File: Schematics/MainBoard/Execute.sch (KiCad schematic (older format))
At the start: 7 parts, among them J23 Control Word LED Connector [1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, J24 Control Word LED Connector [8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, J25 Control Word LED Connector [0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, J5 C Register LED Connector, J6 Control Word LED Connector [2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, U48 74LS245

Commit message: The ALU Carry Input comes from a control signal instead of the C register.
So now:
  * C[0..3] --> S[0..3]
  * C4 --> M
  * ~CarryIn --> Cn
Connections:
- net ControlWord26 renamed ~CarryIn
- no-connect marks 5 -> 4
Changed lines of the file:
@@
 Text GLabel 4850 3800 1    50   Output ~ 0
 ~LinkHiOut
-NoConn ~ 4550 3800
 NoConn ~ 4400 3800
 NoConn ~ 4250 3800
@@
 Wire Wire Line
 	8200 5750 8200 5650
+Text GLabel 4550 3800 1    50   Output ~ 0
+~CarryIn
 Wire Bus Line
 	1100 1050 5850 1050

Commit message: WIP: fix schematic ERC violations.
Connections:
- no-connect marks 4 -> 0
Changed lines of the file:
@@
 ~CO
-$Comp
-L power:VCC #PWR?
-U 1 1 5D915857
-P 1700 7400
-AR Path="/5D2C0761/5D915857" Ref="#PWR?"  Part="1"
-AR Path="/5D2C0B92/5D915857" Ref="#PWR?"  Part="1"
-AR Path="/5D2C13FD/5D915857" Ref="#PWR0132"  Part="1"
-F 0 "#PWR0132" H 1700 7250 50  0001 C CNN
-F 1 "VCC" H 1717 7573 50  0000 C CNN
-F 2 "" H 1700 7400 50  0001 C CNN
-F 3 "" H 1700 7400 50  0001 C CNN
-	1    1700 7400
-	1    0    0    -1
-$EndComp
 $Comp
 L power:GND #PWR?
@@
 	3700 4550 3800 4450
 Entry Wire Line
-	3850 4550 3950 4450
-Entry Wire Line
-	4000 4550 4100 4450
-Entry Wire Line
-	4150 4550 4250 4450
-Entry Wire Line
-	4300 4550 4400 4450
-Entry Wire Line
 	4450 4550 4550 4450
 Entry Wire Line
@@
 	4550 3800 4550 4450
 Wire Wire Line
-	4400 3800 4400 4450
-Wire Wire Line
-	4250 3800 4250 4450
-Wire Wire Line
-	4100 3800 4100 4450
-Wire Wire Line
-	3950 3800 3950 4450
-Wire Wire Line
 	3800 3800 3800 4450
 Text Label 4550 4400 1    50   ~ 0
 ControlWord26
-Text Label 4400 4400 1    50   ~ 0
-ControlWord27
-Text Label 4250 4400 1    50   ~ 0
-ControlWord28
-Text Label 4100 4400 1    50   ~ 0
-ControlWord29
-Text Label 3950 4400 1    50   ~ 0
-ControlWord30
 Text Label 3800 4400 1    50   ~ 0
 ControlWord31
@@
 Text GLabel 4850 3800 1    50   Output ~ 0
 ~LinkHiOut
-NoConn ~ 4400 3800
-NoConn ~ 4250 3800
-NoConn ~ 4100 3800
-NoConn ~ 3950 3800
 $Comp
 L Connector:Conn_01x09_Female J?
@@
 Wire Bus Line
 	1500 5050 8000 5050
+$Comp
+L power:VCC #PWR0132
+U 1 1 5DD28AFB
+P 1700 7400
+F 0 "#PWR0132" H 1700 7250 50  0001 C CNN
+F 1 "VCC" H 1717 7573 50  0000 C CNN
+F 2 "" H 1700 7400 50  0001 C CNN
+F 3 "" H 1700 7400 50  0001 C CNN
+	1    1700 7400
+	1    0    0    -1
+$EndComp
 $EndSCHEMATC

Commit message: Add the Link Register so we can implement microcode for JALR.
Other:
- note added: "There are\nunused control\nsignals here\nfor future\nexpansion."
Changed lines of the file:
@@
 $Descr A 11000 8500
 encoding utf-8
-Sheet 12 22
+Sheet 12 23
 Title "Execute"
 Date ""
@@
 Text GLabel 4550 3800 1    50   Output ~ 0
 ~CarryIn
+$Comp
+L power:VCC #PWR0132
+U 1 1 5DD28AFB
+P 1700 7400
+F 0 "#PWR0132" H 1700 7250 50  0001 C CNN
+F 1 "VCC" H 1717 7573 50  0000 C CNN
+F 2 "" H 1700 7400 50  0001 C CNN
+F 3 "" H 1700 7400 50  0001 C CNN
+	1    1700 7400
+	1    0    0    -1
+$EndComp
 Wire Bus Line
 	1100 1050 5850 1050
@@
 Wire Bus Line
 	1500 5050 8000 5050
-$Comp
-L power:VCC #PWR0132
-U 1 1 5DD28AFB
-P 1700 7400
-F 0 "#PWR0132" H 1700 7250 50  0001 C CNN
-F 1 "VCC" H 1717 7573 50  0000 C CNN
-F 2 "" H 1700 7400 50  0001 C CNN
-F 3 "" H 1700 7400 50  0001 C CNN
-	1    1700 7400
-	1    0    0    -1
-$EndComp
+Text Notes 3900 4250 0    50   ~ 0
+There are\nunused control\nsignals here\nfor future\nexpansion.
 $EndSCHEMATC

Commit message: Rename UVInc and XYInc to mark them as active-high, not active-low.
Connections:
- net ~UVInc renamed UVInc
- net ~XYInc renamed XYInc
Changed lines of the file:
@@
 ~PI
 Text GLabel 6650 3800 1    50   Output ~ 0
-~UVInc
+UVInc
 Text GLabel 6800 3800 1    50   Output ~ 0
 ~VO
@@
 ~MI
 Text GLabel 5600 3800 1    50   Output ~ 0
-~XYInc
+XYInc
 Text GLabel 5750 3800 1    50   Output ~ 0
 ~YO

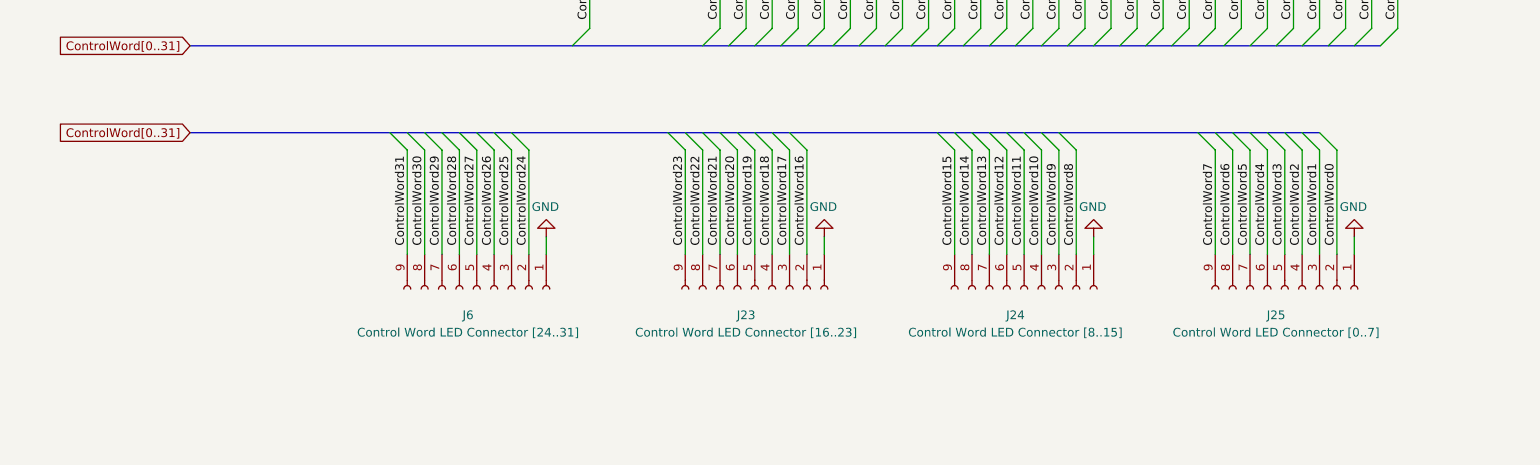
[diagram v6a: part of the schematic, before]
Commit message: Begin work on the Rev 2 hardware.
* Four layer PCB for the main board
* Breaking the main board up into several smaller daughter boaeds.
* ZIF sockets for Instruction ROM
* Dual Port SRAM for Instruction RAM
* Daughter board connectors interleave signals and GND.
* DC Barrel jack connector for power
* WIP shifter circuit
* Rename SharedMemoryArduinoSerialCard to SerialCard.
* TurtleTTL Rev 2 will use the shared memory serial card.
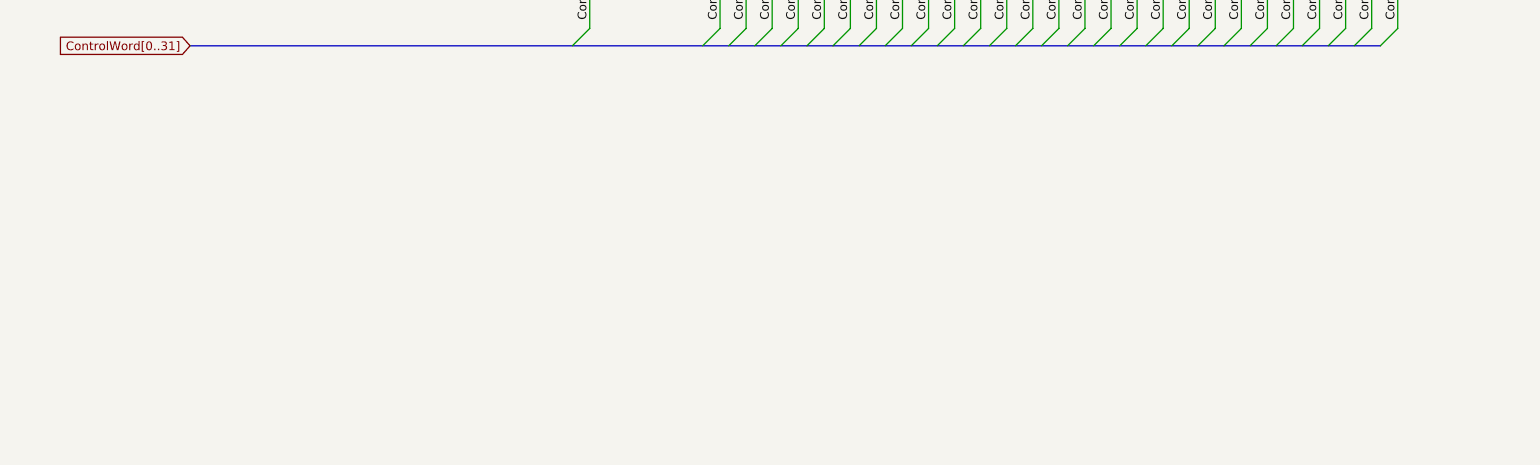
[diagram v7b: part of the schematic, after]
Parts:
- removed J23: Control Word LED Connector [16..23], Connector_PinSocket_2.54mm:PinSocket_1x09_P2.54mm_Vertical, symbol Connector:Conn_01x09_Female
- removed J24: Control Word LED Connector [8..15], Connector_PinSocket_2.54mm:PinSocket_1x09_P2.54mm_Vertical, symbol Connector:Conn_01x09_Female
- removed J25: Control Word LED Connector [0..7], Connector_PinSocket_2.54mm:PinSocket_1x09_P2.54mm_Vertical, symbol Connector:Conn_01x09_Female
- removed J6: Control Word LED Connector [24..31], Connector_PinSocket_2.54mm:PinSocket_1x09_P2.54mm_Vertical, symbol Connector:Conn_01x09_Female
